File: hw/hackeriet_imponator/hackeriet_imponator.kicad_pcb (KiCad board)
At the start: 2 copper layers, 70 x 70 mm, 25 parts, among them J1 USB4085-GF-A, J2 UPDI Programming, J3 External Battery Connector, J4 Shitty Add On, J5 Unused pins, SW1 SW_SPDT, U1 ATtiny804-SS, U2 MCP2221AxSL

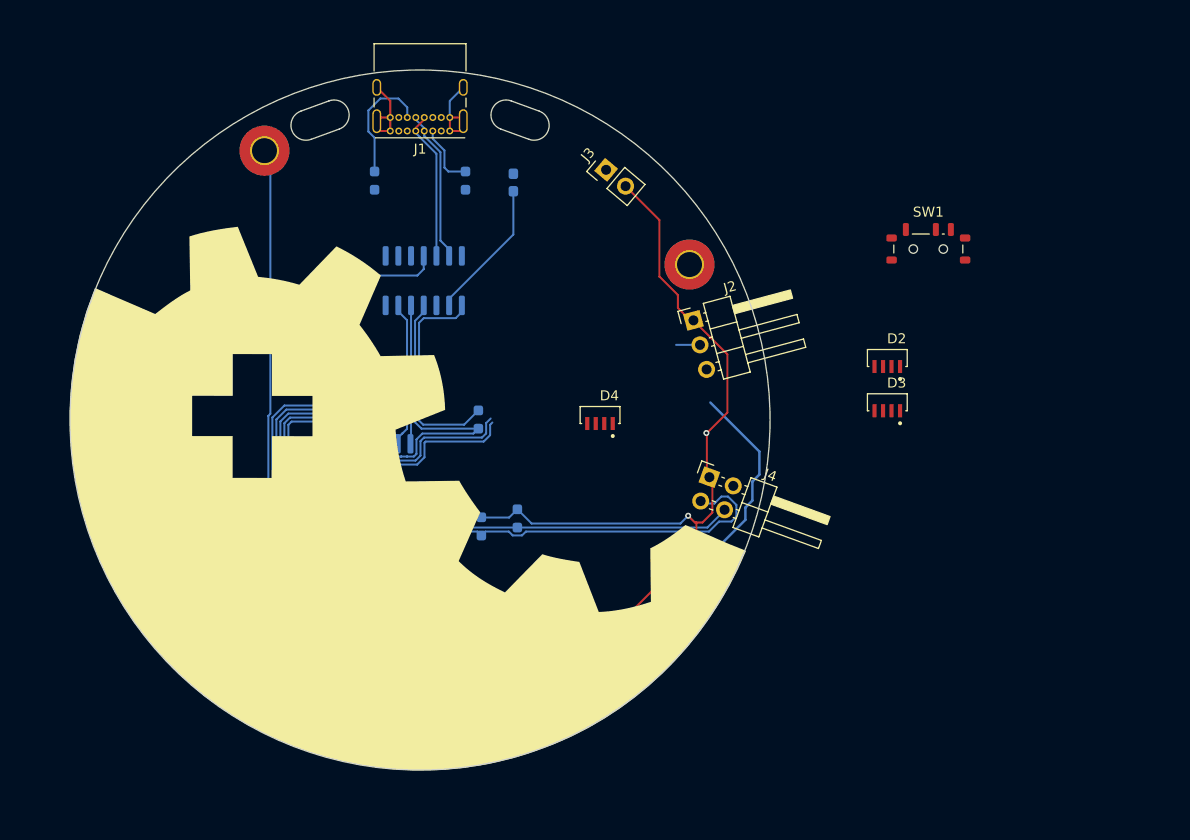
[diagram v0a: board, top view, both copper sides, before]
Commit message: Fine-tuned silkscreen logo and LED spacing.
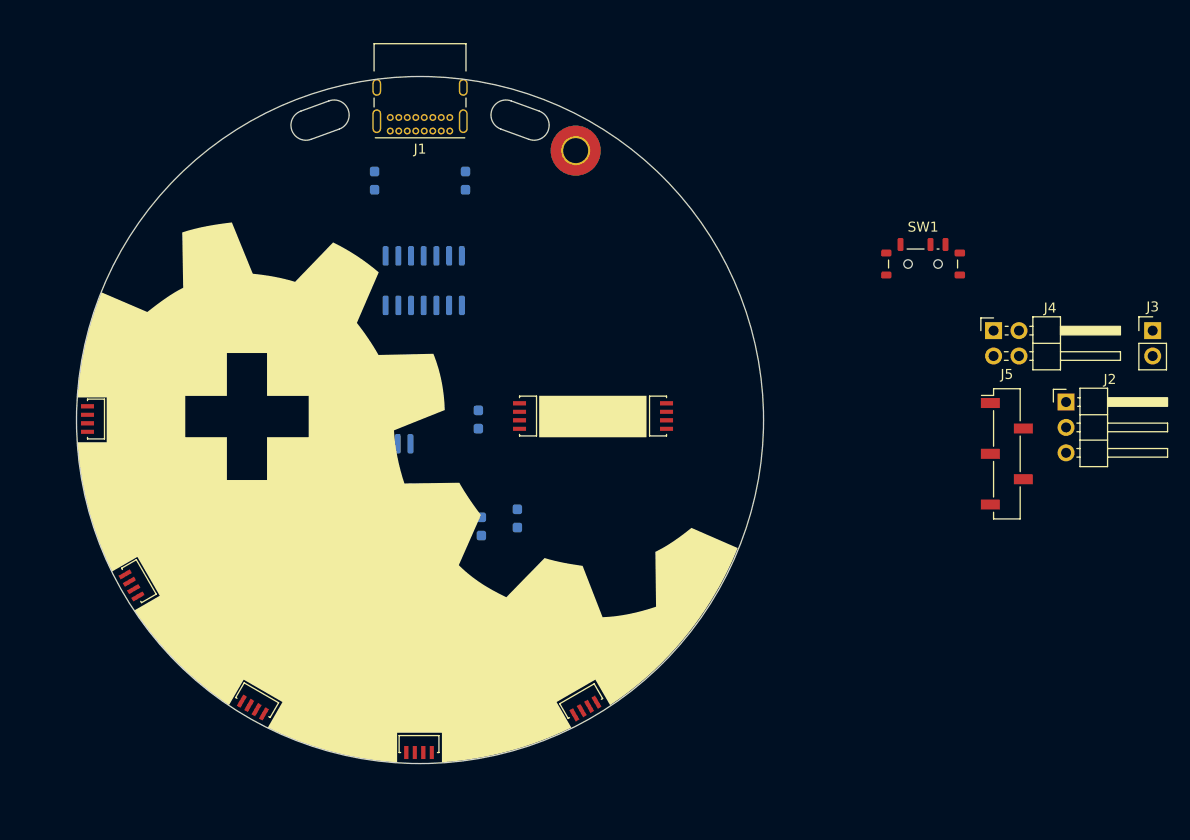
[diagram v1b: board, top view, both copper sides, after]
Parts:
- removed H1: M2, BATT, MountingHole:MountingHole_2.5mm_Pad_TopBottom
- added D5: WS2812B, imponator_footprint_lib:LED_WS2812B-4020, F.Cu at (149.8, 118.8)
- added D6: WS2812B, imponator_footprint_lib:LED_WS2812B-4020, F.Cu at (157.5, 90.3)
- added D7: WS2812B, imponator_footprint_lib:LED_WS2812B-4020, F.Cu at (144.5, 90.3)
- D1: value Rx LED -> WS2812B; footprint LED_SMD:LED_0603_1608Metric_Pad1.05x0.95mm_HandSolder -> imponator_footprint_lib:LED_WS2812B-4020; moved to F.Cu
- J5: moved to F.Cu
- R1, R2: value 5.1K -> 4.7K
- R3: value 10k -> 5.1K
- R4: value 4.7K -> 5.1K
- R5: value 4.7K -> 10k
- moved D2 78.1 mm to (105.6, 106.8), turned to -60 degrees
- moved J5 73.2 mm to (192.3, 94.0), turned to 0 degrees
- moved D3 69.7 mm to (117.4, 118.7), turned to -30 degrees
- moved J3 57.0 mm to (206.9, 81.7), turned to 0 degrees
- moved D1 48.0 mm to (101.3, 90.6)
- moved J2 38.1 mm to (198.3, 88.9), turned to 0 degrees
- moved D4 37.6 mm to (133.6, 123.1)
- moved J4 32.0 mm to (191.0, 81.7), turned to 0 degrees
- moved H4 16.1 mm to (149.2, 63.7)
- moved H3 8.12 mm to (103.6, 98.7), turned to -30 degrees
- moved H2 8.12 mm to (141.7, 120.7), turned to -30 degrees
- moved SW1 1.59 mm to (184.0, 75.1)
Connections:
- D1 pad 1: GND -> VDD
- D1 pad 2: Net-(D1-A) -> Net-(D1-DOUT)
- D2 pad 4: WS2812B LED RGB Control -> Net-(D1-DOUT)
- D4 pad 2: unconnected-(D4-DOUT-Pad2) -> Net-(D4-DOUT)
- R1 pad 1: Net-(J1-CC1) -> VDD
- R1 pad 2: GND -> SCL
- R2 pad 1: Net-(J1-CC2) -> VDD
- R2 pad 2: GND -> SDA
- R3 pad 1: VDD -> Net-(J1-CC1)
- R3 pad 2: MCP2221 _RST -> GND
- R4 pad 1: VDD -> Net-(J1-CC2)
- R4 pad 2: SCL -> GND
- R5 pad 2: SDA -> MCP2221 _RST
- U2 pad 2: Net-(D1-A) -> unconnected-(U2-GP0-Pad2)
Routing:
- net BATT: track 204.5 -> 0.00 mm, vias 4 -> 0
- net PA3: track 47.3 -> 0.00 mm
- net PA7: track 42.5 -> 0.00 mm
- net SCL: track 42.5 -> 0.00 mm
- net PA5: track 41.7 -> 0.00 mm
- net PA6: track 39.1 -> 0.00 mm
- net PA4: track 39.0 -> 0.00 mm
- net RGB DOUT, to top PCB: track 38.3 -> 0.00 mm
- net SDA: track 34.5 -> 0.00 mm
- net MCP2221 _RST: track 34.5 -> 0.00 mm
- net VDD: track 22.3 -> 0.00 mm
- net GND: track 19.0 -> 0.00 mm
- net Net-(J2-Pin_2): track 18.3 -> 0.00 mm
- net WS2812B LED RGB Control: track 16.8 -> 0.00 mm
- net D+: track 15.4 -> 0.00 mm
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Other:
- board size 70 x 70 mm -> 68.7 x 68.7 mm

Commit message: Fixed LED pinout. Added PCB button. Distributed headers along side.
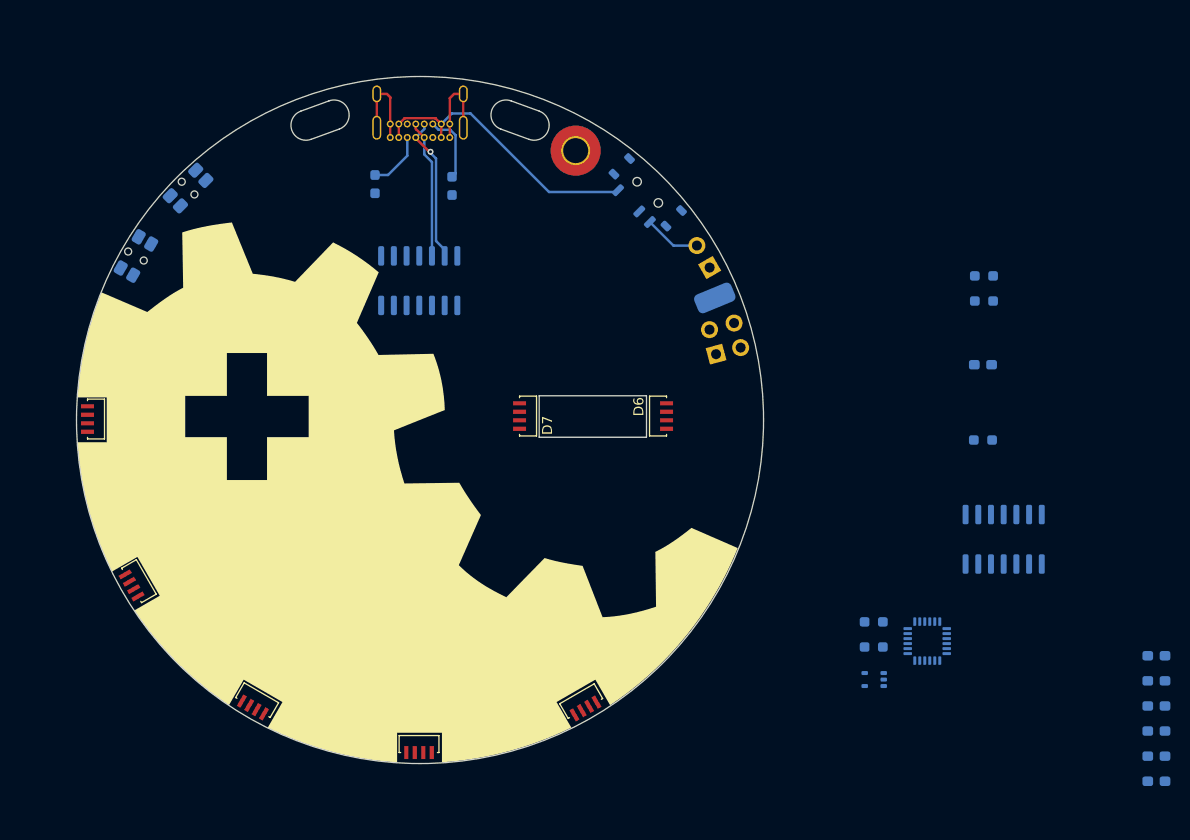
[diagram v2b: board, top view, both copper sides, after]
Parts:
- removed the D1 at (101.3, 90.6)
- added C3: 2.2nF, Capacitor_SMD:C_0603_1608Metric_Pad1.08x0.95mm_HandSolder, B.Cu at (207.3, 114.2)
- added C4: 0.1uF, Capacitor_SMD:C_0603_1608Metric_Pad1.08x0.95mm_HandSolder, B.Cu at (207.3, 116.7)
- added C5: 0.1uF, Capacitor_SMD:C_0603_1608Metric_Pad1.08x0.95mm_HandSolder, B.Cu at (207.3, 119.2)
- added C6: 10nF, Capacitor_SMD:C_0603_1608Metric_Pad1.08x0.95mm_HandSolder, B.Cu at (207.3, 121.8)
- added C7: 1uF, Capacitor_SMD:C_0603_1608Metric_Pad1.08x0.95mm_HandSolder, B.Cu at (207.3, 124.3)
- added C8: 1uF, Capacitor_SMD:C_0603_1608Metric_Pad1.08x0.95mm_HandSolder, B.Cu at (207.3, 126.8)
- added D5: WS2812B-4020, imponator_footprint_lib:LED_WS2812B-4020, F.Cu at (101.3, 90.6)
- added R6: 0R, Resistor_SMD:R_0603_1608Metric_Pad0.98x0.95mm_HandSolder, B.Cu at (179.0, 110.8)
- added R7: 0R, Resistor_SMD:R_0603_1608Metric_Pad0.98x0.95mm_HandSolder, B.Cu at (179.0, 113.4)
- added SW2: User configurable, Button_Switch_SMD:SW_SPST_EVQP7C, B.Cu at (105.3, 74.3)
- added SW3: User configurable, Button_Switch_SMD:SW_SPST_EVQP7C, B.Cu at (110.5, 67.5)
- added U3: MPU-6050, Sensor_Motion:InvenSense_QFN-24_4x4mm_P0.5mm, B.Cu at (184.4, 112.8)
- added U4: TLV70028_SOT353, Package_TO_SOT_SMD:SOT-353_SC-70-5, B.Cu at (179.1, 116.6)
- D1: renamed from D5; value WS2812B -> WS2812B-4020
- D2: renamed from D4; value WS2812B -> WS2812B-4020
- D3, D6, D7: value WS2812B -> WS2812B-4020
- D4: renamed from D2; value WS2812B -> WS2812B-4020
- J1, J3, J4, SW1: moved to B.Cu
- J2: value UPDI Programming -> UPDI programming; footprint Connector_PinHeader_2.54mm:PinHeader_1x03_P2.54mm_Horizontal -> Connector_Wire:SolderWirePad_1x01_SMD_2x4mm; moved to B.Cu
- J5: footprint Connector_PinSocket_2.54mm:PinSocket_1x05_P2.54mm_Vertical_SMD_Pin1Left -> Connector_PinSocket_2.54mm:PinSocket_1x02_P2.54mm_Vertical_SMD_Pin1Right; moved to B.Cu
- moved J5 89.5 mm to (103.6, 82.6), turned to 165 degrees
- moved C1 68.8 mm to (190.0, 85.1), turned to 180 degrees
- moved U1 63.5 mm to (192.0, 102.6)
- moved R2 62.1 mm to (190.1, 78.8), turned to 180 degrees
- moved R1 52.7 mm to (190.1, 76.2), turned to 180 degrees
- moved R5 47.2 mm to (190.0, 92.7), turned to 180 degrees
- moved J3 44.7 mm to (162.6, 75.4), turned to 30 degrees
- moved J2 36.6 mm to (163.1, 78.5), turned to 112.5 degrees
- moved R4 34.2 mm to (136.9, 67.2)
- moved SW1 28.4 mm to (156.4, 67.9), turned to -45 degrees
- moved J4 27.8 mm to (163.3, 84.1), turned to 15 degrees
- moved R3 25.7 mm to (129.2, 67.1)
- moved J1 5.99 mm to (130.7, 62.4), turned to 0 degrees
- moved U2 0.45 mm to (133.6, 76.7)
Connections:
- D1 pad 1: VDD -> WS2812B LED RGB Control
- D1 pad 2: Net-(D5-DOUT) -> VDD
- D1 pad 3: GND -> Net-(D1-DOUT)
- D1 pad 4: Net-(D4-DOUT) -> GND
- D2 pad 1: VDD -> Net-(D1-DOUT)
- D2 pad 2: Net-(D4-DOUT) -> VDD
- D2 pad 3: GND -> Net-(D2-DOUT)
- D2 pad 4: Net-(D3-DOUT) -> GND
- D3 pad 1: VDD -> Net-(D2-DOUT)
- D3 pad 2: Net-(D3-DOUT) -> VDD
- D3 pad 3: GND -> Net-(D3-DOUT)
- D3 pad 4: Net-(D2-DOUT) -> GND
- D4 pad 1: VDD -> Net-(D3-DOUT)
- D4 pad 2: Net-(D2-DOUT) -> VDD
- D4 pad 3: GND -> Net-(D4-DOUT)
- D4 pad 4: Net-(D1-DOUT) -> GND
- D6 pad 1: VDD -> WS2812B LED RGB Control minus
- D6 pad 2: Net-(D6-DOUT) -> VDD
- D6 pad 3: GND -> Net-(D6-DOUT)
- D6 pad 4: Net-(D5-DOUT) -> GND
- D7 pad 1: VDD -> Net-(D6-DOUT)
- D7 pad 2: unconnected-(D7-DOUT-Pad2) -> VDD
- D7 pad 3: GND -> unconnected-(D7-DOUT-Pad3)
- D7 pad 4: Net-(D6-DOUT) -> GND
- J2 pad 1: VDD -> Net-(J2-Pin_1)
- J5 pad 1: unconnected-(J5-Pin_1-Pad1) -> ACC_INT
- J5 pad 2: unconnected-(J5-Pin_2-Pad2) -> ACC_ENABLE
- U1 pad 10: Net-(J2-Pin_2) -> Net-(J2-Pin_1)
- U1 pad 11: WS2812B LED RGB Control -> WS2812B LED RGB Control plate
- U1 pad 12: MCP2221 _RST -> WS2812B LED RGB Control minus
- U1 pad 13: PA3 -> Net-(U1-PA3)
- U1 pad 2: PA4 -> Net-(U1-PA4)
- U1 pad 3: PA5 -> ACC_INT
- U1 pad 4: PA6 -> ACC_ENABLE
- U1 pad 5: PA7 -> MCP2221 _RST
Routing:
- net USB_VDD: track 0.00 -> 28.9 mm
- net GND: track 0.00 -> 17.7 mm
- net D+: track 0.00 -> 14.8 mm, vias 0 -> 1
- net D-: track 0.00 -> 13.9 mm
- net Net-(J1-CC2): track 0.00 -> 7.05 mm
- net Net-(J1-CC1): track 0.00 -> 5.85 mm
- net BATT: track 0.00 -> 5.68 mm
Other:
- outline, holes or cut-outs redrawn

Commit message: Did a bunch of routing and changed holes. Also some silk
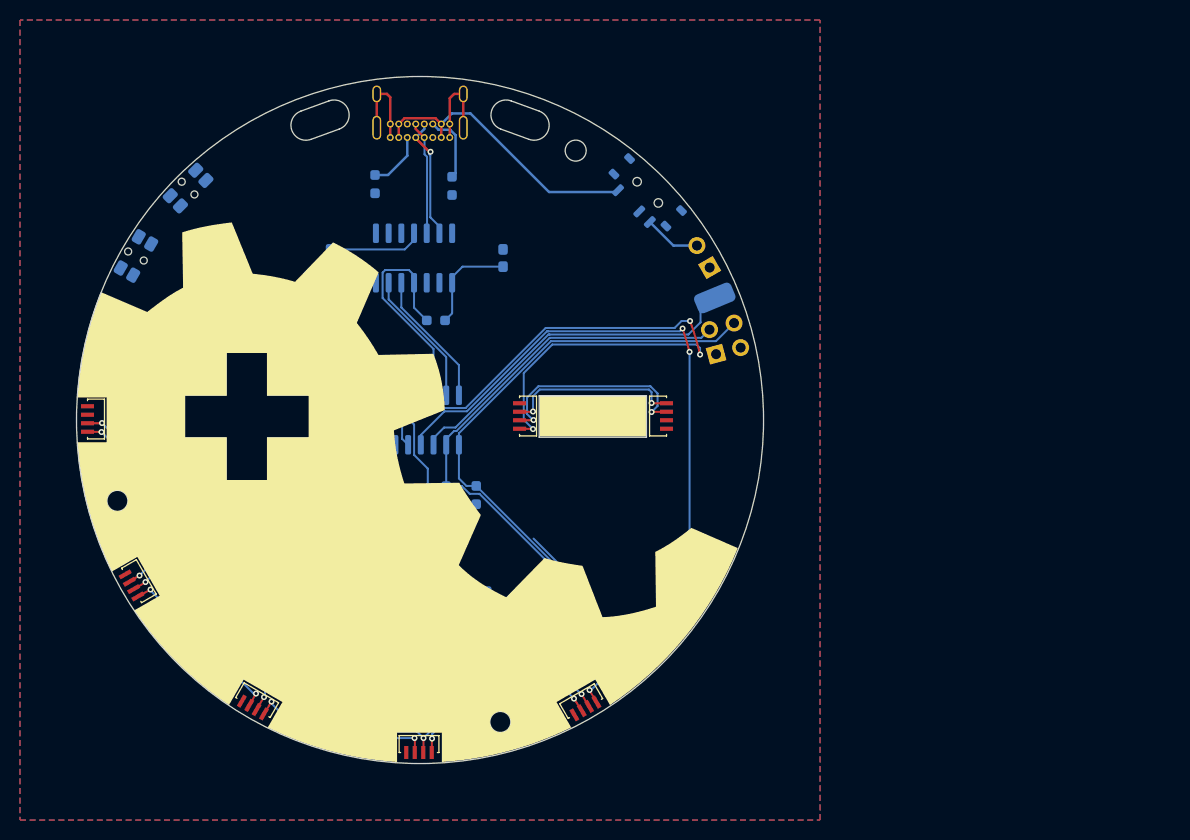
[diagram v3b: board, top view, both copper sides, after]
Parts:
- removed H2: M2 DOUT, MountingHole:MountingHole_2.5mm_Pad_TopBottom
- removed H3, H4: M2 GND, MountingHole:MountingHole_2.5mm_Pad_TopBottom
- added C9: 100nF, Capacitor_SMD:C_0603_1608Metric_Pad1.08x0.95mm_HandSolder, B.Cu at (142.0, 74.5)
- added REF**: MountingHole_2.1mm, MountingHole:MountingHole_2.1mm, B.Cu at (149.2, 63.7)
- added REF**: MountingHole_2.1mm, MountingHole:MountingHole_2.1mm, B.Cu at (103.4, 98.7)
- added REF**: MountingHole_2.1mm, MountingHole:MountingHole_2.1mm, B.Cu at (141.7, 120.8)
- moved C8 86.6 mm to (121.7, 113.7), turned to 90 degrees
- moved C7 77.6 mm to (130.4, 113.7), turned to 90 degrees
- moved C6 74.4 mm to (133.3, 113.7), turned to -90 degrees
- moved C4 74.3 mm to (133.3, 109.6), turned to 90 degrees
- moved C5 68.8 mm to (139.4, 107.8)
- moved C1 65.0 mm to (125.2, 90.6), turned to 90 degrees
- moved C3 60.6 mm to (146.7, 113.7), turned to 90 degrees
- moved U1 59.5 mm to (133.7, 90.7)
- moved R1 58.1 mm to (136.3, 98.2), turned to 90 degrees
- moved R5 56.0 mm to (135.3, 80.7)
- moved R6 55.0 mm to (124.0, 109.6), turned to -90 degrees
- moved R2 54.3 mm to (139.3, 98.2), turned to 90 degrees
- moved U4 53.1 mm to (126.0, 113.6), turned to 0 degrees
- moved R7 52.5 mm to (126.6, 109.6), turned to -90 degrees
- moved U3 45.0 mm to (139.4, 113.7), turned to 90 degrees
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- renumbered D7 to D6, D6 to D7
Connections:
- D1 pad 1: WS2812B LED RGB Control -> WS2812B LED RGB Control logo
- D6 pad 1: Net-(D6-DOUT) -> WS2812B LED RGB Control minus
- D6 pad 3: unconnected-(D7-DOUT-Pad3) -> Net-(D6-DOUT)
- D7 pad 1: WS2812B LED RGB Control minus -> Net-(D6-DOUT)
- D7 pad 3: Net-(D6-DOUT) -> unconnected-(D7-DOUT-Pad3)
- U1 pad 11: WS2812B LED RGB Control plate -> WS2812B LED RGB Control logo
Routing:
- net VDD: track 0.00 -> 134.4 mm, vias 0 -> 7
- net WS2812B LED RGB Control logo: track 0.00 -> 69.6 mm, vias 0 -> 3
- net WS2812B LED RGB Control minus: track 0.00 -> 67.9 mm, vias 0 -> 3
- net SDA: track 0.00 -> 66.5 mm
- net SCL: track 0.00 -> 64.4 mm
- net Net-(J2-Pin_1): track 0.00 -> 35.8 mm
- net ACC_ENABLE: track 0.00 -> 28.7 mm
- net ACC_INT: track 0.00 -> 27.1 mm
- net MCP2221 _RST: track 0.00 -> 22.9 mm
- net Net-(D1-DOUT): track 0.00 -> 18.8 mm, vias 0 -> 2
- net Net-(D4-DOUT): track 0.00 -> 18.0 mm, vias 0 -> 2
- net Net-(D6-DOUT): track 0.00 -> 17.7 mm, vias 0 -> 2
- net Net-(D2-DOUT): track 0.00 -> 17.4 mm, vias 0 -> 2
- net Net-(D3-DOUT): track 0.00 -> 14.9 mm, vias 0 -> 2
- net Net-(U3-VDD): track 0.00 -> 14.7 mm
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- added copper zone on B.Cu, net GND
- added copper zone on F.Cu, net GND
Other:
- board text added: "MCU: ATtiny804"
- board text added: "Optional: Accelerometer MPU-6050"
- board text added: "USB to UART module"
- board text removed: "BATT"
- board text removed: "DATA"
- board text removed: "External Battery Connector"
- board text removed: "Shitty Add-on"

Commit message: More routing
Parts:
- turned C3 to -90 degrees
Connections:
- SW2 pad 1: Net-(U1-PA3) -> Net-(U1-PA5)
- SW3 pad 1: Net-(U1-PA4) -> Net-(U1-PA6)
- U1 pad 13: Net-(U1-PA3) -> ACC_INT
- U1 pad 2: Net-(U1-PA4) -> ACC_ENABLE
- U1 pad 3: ACC_INT -> Net-(U1-PA5)
- U1 pad 4: ACC_ENABLE -> Net-(U1-PA6)
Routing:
- net ACC_INT: track 27.1 -> 74.3 mm
- net Net-(U1-PA5): track 0.00 -> 40.1 mm
- net Net-(U1-PA6): track 0.00 -> 35.0 mm
- net WS2812B LED RGB Control logo: track 69.6 -> 35.4 mm, vias 3 -> 5
- net Net-(D1-DOUT): track 18.8 -> 1.41 mm
- net Net-(D4-DOUT): track 18.0 -> 1.41 mm
- net Net-(D2-DOUT): track 17.4 -> 1.53 mm
- net Net-(D3-DOUT): track 14.9 -> 0.10 mm
- net WS2812B LED RGB Control minus: track 67.9 -> 60.4 mm
- net VDD: track 134.4 -> 130.7 mm
- net SCL: track 64.4 -> 67.0 mm
- net Net-(U3-CPOUT): track 5.40 -> 7.41 mm
- net SDA: track 66.5 -> 67.3 mm
- net ACC_ENABLE: track 28.7 -> 29.3 mm

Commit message: Added Logic Level Converter. Added GND vias. Routed the rest. Ran Design Rules test and fixed stuff.
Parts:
- removed J5: Unused pins, Connector_PinSocket_2.54mm:PinSocket_1x02_P2.54mm_Vertical_SMD_Pin1Right
- removed R1, R2: 4.7K, Resistor_SMD:R_0603_1608Metric_Pad0.98x0.95mm_HandSolder
- added Q1: AO3400A, Package_TO_SOT_SMD:SOT-23, B.Cu at (139.4, 101.7)
- added Q2: AO3400A, Package_TO_SOT_SMD:SOT-23, B.Cu at (130.5, 101.7)
- added R10: 10k, Resistor_SMD:R_0603_1608Metric_Pad0.98x0.95mm_HandSolder, B.Cu at (133.1, 99.7)
- added R11: 10k, Resistor_SMD:R_0603_1608Metric_Pad0.98x0.95mm_HandSolder, B.Cu at (130.5, 105.8)
- added R8: 10k, Resistor_SMD:R_0603_1608Metric_Pad0.98x0.95mm_HandSolder, B.Cu at (136.9, 99.7)
- added R9: 10k, Resistor_SMD:R_0603_1608Metric_Pad0.98x0.95mm_HandSolder, B.Cu at (139.4, 105.8)
- added REF**: TestPoint_Pad_2.0x2.0mm, TestPoint:TestPoint_Pad_2.0x2.0mm, B.Cu at (121.5, 99.5)
- added REF**: TestPoint_Pad_2.0x2.0mm, TestPoint:TestPoint_Pad_2.0x2.0mm, B.Cu at (126.8, 99.5)
- moved C5 0.40 mm to (139.4, 108.2)
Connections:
- net Net-(U3-VDD) renamed 2V8
- U3 pad 23: SCL -> Net-(Q2-S)
- U3 pad 24: SDA -> Net-(Q1-S)
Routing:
- net 2V8: track 14.7 -> 82.7 mm
- net ACC_INT: track 74.3 -> 29.6 mm
- net Net-(Q2-S): track 0.00 -> 33.7 mm
- net Net-(Q1-S): track 0.00 -> 25.9 mm
- net SDA: track 67.3 -> 41.7 mm
- net SCL: track 67.0 -> 46.3 mm
- net GND: track 23.3 -> 35.8 mm, vias 0 -> 8
- net VDD: track 130.7 -> 143.1 mm, vias 7 -> 8
- net ACC_ENABLE: track 29.3 -> 31.9 mm
- net USB_VDD: track 28.9 -> 29.9 mm
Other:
- board text removed: "${REFERENCE}"

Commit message: Cleaned up silkscreen. Added some more silkscreen stuff.
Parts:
- J4: value Shitty Add On -> Shitty Add-On
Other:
- board text added: "0"
- board text added: "10"
- board text added: "100"
- board text added: "110"
- board text added: "150"
- board text added: "180"
- board text added: "20"
- board text added: "30"
- board text added: "40"
- board text added: "50"
- board text added: "60"
- board text added: "70"
- board text added: "80"
- board text added: "90"
- board text added: "BATT GND"
- board text added: "https://github.com/hackeriet/imponator Version: 2"
- board text removed: "GND"
